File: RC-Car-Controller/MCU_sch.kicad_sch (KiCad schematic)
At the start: 15 parts, among them SW1 SW_Push, U7 STM32H743VGTx, Y1 Crystal

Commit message: Fixed Controller PCB
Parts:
- added C21: 2.2uF/10V, Capacitor_SMD:C_0201_0603Metric, symbol Device:C
- C10, C11, C12, C34, C35, C36, C7, C8, C9: footprint (none) -> Capacitor_SMD:C_0201_0603Metric
- C40: value 22uF/10V -> 2.2uF/10V; footprint (none) -> Capacitor_SMD:C_0201_0603Metric
- R11, R12: footprint (none) -> Resistor_SMD:R_0201_0603Metric
- SW1: footprint (none) -> Button_Switch_THT:SW_SPST_Omron_B3F-40xx
- Y1: footprint (none) -> Crystal:Crystal_SMD_Abracon_ABM3-2Pin_5.0x3.2mm
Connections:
- net +3V3: now also U7.20 (VREF+)
- net GND_3V3: now also C21.2
- net LEFT_PWM1: now reaches U7.22 (PA0)
- net LEFT_EN1: now reaches U7.23 (PA1)
- net LEFT_PWM2: now reaches U7.24 (PA2)
- net LEFT_EN2: now reaches U7.25 (PA3)
- net at C40.1, U7.73 (VCAP): no longer U7.48 (VCAP)
- net RIGHT_PWM1: now reaches U7.59 (PD12)
- net RIGHT_EN1: now reaches U7.60 (PD13)
- net RIGHT_PWM2: now reaches U7.89 (PB3)
- net RIGHT_EN2: now reaches U7.90 (PB4)
- net RELAY_CTRL: now reaches U7.93 (PB7)
- new net: C21.1, U7.48 (VCAP)
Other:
- moved on the sheet: C10, C11, C12, C7, C8, C9

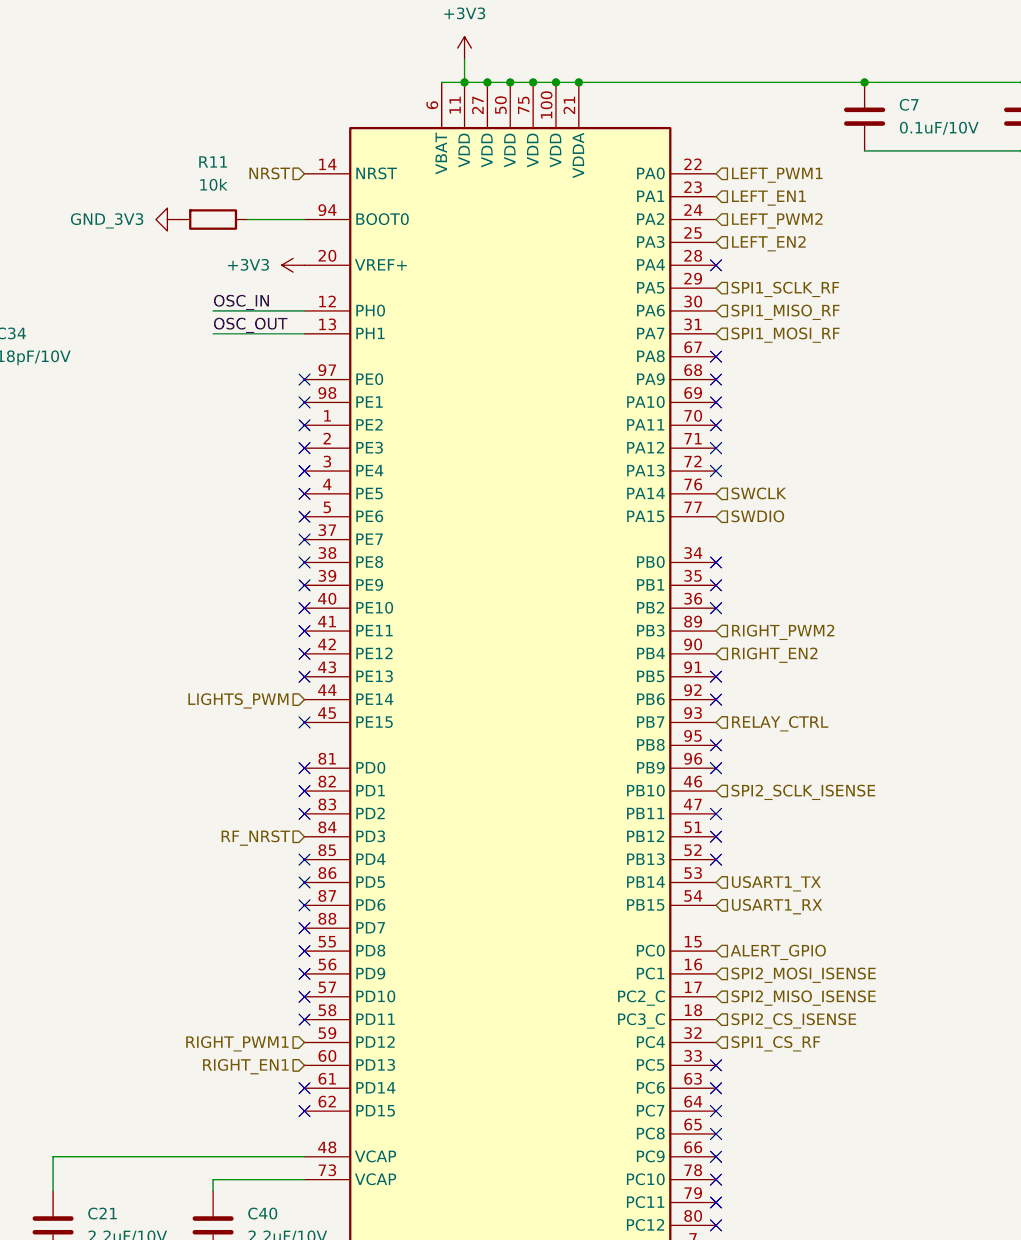
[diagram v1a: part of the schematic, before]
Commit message: Added IO to Controller
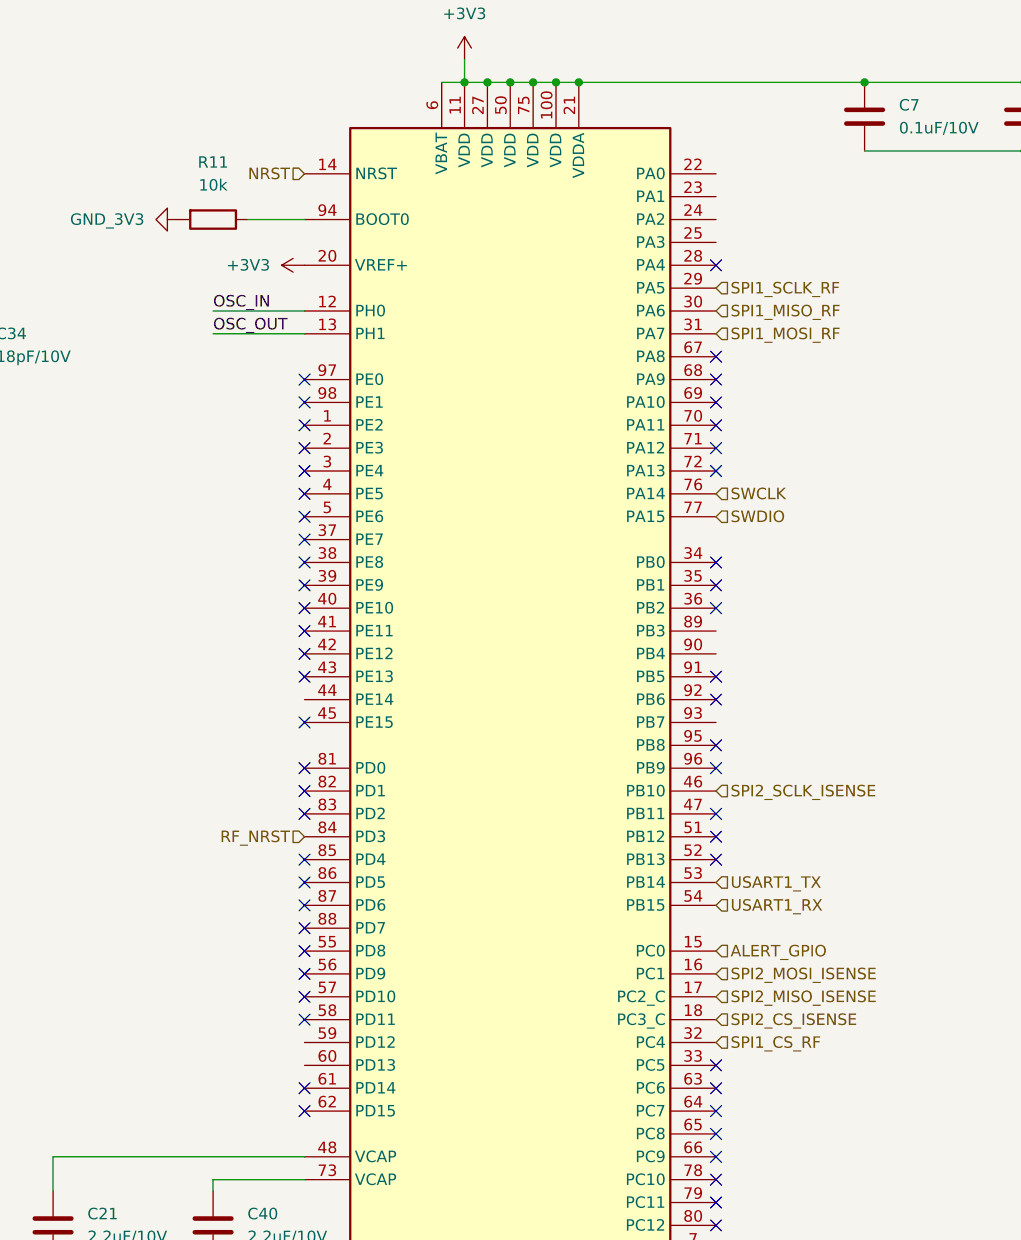
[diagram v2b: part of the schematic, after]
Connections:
- net LEFT_EN1: no longer names the net of U7.23 (PA1)
- net LEFT_EN2: no longer names the net of U7.25 (PA3)
- net LEFT_PWM1: no longer names the net of U7.22 (PA0)
- net LEFT_PWM2: no longer names the net of U7.24 (PA2)
- net LIGHTS_PWM: no longer names the net of U7.44 (PE14)
- net RELAY_CTRL: no longer names the net of U7.93 (PB7)
- net RIGHT_EN1: no longer names the net of U7.60 (PD13)
- net RIGHT_EN2: no longer names the net of U7.90 (PB4)
- net RIGHT_PWM1: no longer names the net of U7.59 (PD12)
- net RIGHT_PWM2: no longer names the net of U7.89 (PB3)
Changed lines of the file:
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@@
-		)
-	)
-	(hierarchical_label "RIGHT_PWM2"
-		(shape input)
-		(at 162.56 82.55 0)
-		(fields_autoplaced yes)
-		(effects
-			(font
-				(size 1.27 1.27)
-			)
-			(justify left)
 		)
 	)
@@
 		)
 	)
-	(hierarchical_label "RIGHT_EN2"
-		(shape input)
-		(at 162.56 85.09 0)
-		(fields_autoplaced yes)
-		(effects
-			(font
-				(size 1.27 1.27)
-			)
-			(justify left)
-		)
-	)
 	(hierarchical_label "SPI2_SCLK_ISENSE"
 		(shape input)
 		(at 162.56 100.33 0)
-		(fields_autoplaced yes)
-		(effects
-			(font
-				(size 1.27 1.27)
-			)
-			(justify left)
-		)
-	)
-	(hierarchical_label "LEFT_PWM2"
-		(shape input)
-		(at 162.56 36.83 0)
-		(fields_autoplaced yes)
-		(effects
-			(font
-				(size 1.27 1.27)
-			)
-			(justify left)
-		)
-	)
-	(hierarchical_label "LEFT_EN2"
-		(shape input)
-		(at 162.56 39.37 0)
 		(fields_autoplaced yes)
 		(effects
@@
 		)
 	)
-	(hierarchical_label "LEFT_PWM1"
-		(shape input)
-		(at 162.56 31.75 0)
-		(fields_autoplaced yes)
-		(effects
-			(font
-				(size 1.27 1.27)
-			)
-			(justify left)
-		)
-	)
-	(hierarchical_label "RIGHT_PWM1"
-		(shape input)
-		(at 116.84 128.27 180)
-		(fields_autoplaced yes)
-		(effects
-			(font
-				(size 1.27 1.27)
-			)
-			(justify right)
-		)
-	)
-	(hierarchical_label "LIGHTS_PWM"
-		(shape input)
-		(at 116.84 90.17 180)
-		(fields_autoplaced yes)
-		(effects
-			(font
-				(size 1.27 1.27)
-			)
-			(justify right)
-		)
-	)
-	(hierarchical_label "LEFT_EN1"
-		(shape input)
-		(at 162.56 34.29 0)
-		(fields_autoplaced yes)
-		(effects
-			(font
-				(size 1.27 1.27)
-			)
-			(justify left)
-		)
-	)
-	(hierarchical_label "RELAY_CTRL"
-		(shape input)
-		(at 162.56 92.71 0)
-		(fields_autoplaced yes)
-		(effects
-			(font
-				(size 1.27 1.27)
-			)
-			(justify left)
-		)
-	)
-	(hierarchical_label "RIGHT_EN1"
-		(shape input)
-		(at 116.84 130.81 180)
-		(fields_autoplaced yes)
-		(effects
-			(font
-				(size 1.27 1.27)
-			)
-			(justify right)
-		)
-	)

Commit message: Finished prelim. Controller
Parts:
- removed C34, C35, C36: 18pF/10V, Capacitor_SMD:C_0201_0603Metric, symbol Device:C
- removed C40: 2.2uF/10V, Capacitor_SMD:C_0201_0603Metric, symbol Device:C
- removed U7: STM32H743VGTx, Package_QFP:LQFP-100_14x14mm_P0.5mm, symbol MCU_ST_STM32H7:STM32H743VGTx
- added C13: 0.1uF/10V, Capacitor_SMD:C_0201_0603Metric, symbol Device:C
- added C4, C5, C6: 18pF/10V, Capacitor_SMD:C_0201_0603Metric, symbol Device:C
- added U4: STM32H743VGTx, Package_QFP:LQFP-100_14x14mm_P0.5mm, symbol MCU_ST_STM32H7:STM32H743VGTx
- C21: value 2.2uF/10V -> 0.1uF/10V
- C7, C8: value 0.1uF/10V -> 2.2uF/10V
- R11: value 10k -> 10kohm
- R12: value 10kohm -> 10k
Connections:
- net +3V3: now also C21.1, R11.1, C13.1, U4.100 (VDD), U4.11 (VDD), U4.20 (VREF+), U4.21 (VDDA), U4.27 (VDD), U4.50 (VDD), U4.6 (VBAT), U4.75 (VDD); no longer C7.1, C8.1, R12.1
- net ALERT_GPIO: now also U4.15 (PC0)
- net GND_3V3: now also R12.2, C13.2, C4.2, C5.2, C6.2, U4.10 (VSS), U4.19 (VSSA), U4.26 (VSS), U4.49 (VSS), U4.74 (VSS), U4.99 (VSS); no longer R11.2
- net NRST: now also R11.2, C5.1, U4.14 (NRST); no longer R12.2
- net OSC_IN: now also C4.1, U4.12 (PH0)
- net OSC_OUT: now also C6.1, U4.13 (PH1)
- net RF_NRST: now also U4.40 (PE10)
- net SWCLK: now also U4.76 (PA14)
- net SWDIO: now also U4.77 (PA15)
- net USART1_RX: now also U4.54 (PB15)
- net USART1_TX: now also U4.53 (PB14)
- new net: R12.1, U4.94 (BOOT0)
- new net: C7.1, U4.48 (VCAP)
- new net: C8.1, U4.73 (VCAP)
- new net BTN_L: U4.81 (PD0)
- new net BTN_R: U4.82 (PD1)
- new net I2C1_SCL: U4.92 (PB6)
- new net I2C1_SDA: U4.96 (PB9)
- new net I2C2_SCL: U4.46 (PB10)
- new net I2C2_SDA: U4.47 (PB11)
- new net SPI2_CS_LCD: U4.18 (PC3_C)
- new net SPI2_MISO: U4.17 (PC2_C)
- new net SPI2_MOSI: U4.16 (PC1)
- new net SPI2_SCLK: U4.52 (PB13)
- new net SPI3_CS_ADC: U4.80 (PC12)
- new net SPI3_MISO: U4.79 (PC11)
- new net SPI3_MOSI: U4.36 (PB2)
- new net SPI3_SCLK: U4.78 (PC10)
- new net SPI4_CS_RF: U4.41 (PE11)
- new net SPI4_MISO_RF: U4.43 (PE13)
- new net SPI4_MOSI_RF: U4.5 (PE6)
- new net SPI4_SCLK_RF: U4.42 (PE12)
- new net WIPE_L: U4.31 (PA7)
- new net WIPE_R: U4.34 (PB0)
- no-connect marks 56 -> 54

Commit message: Did some stuff on the Controller
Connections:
- net at R12.1: no longer U4.94 (BOOT0)
- net MCU_USB_D-: now reaches U4.70 (PA11)
- net MCU_USB_D+: now reaches U4.71 (PA12)
- no-connect marks 54 -> 52
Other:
- note added: "Turn this into a DIP Switch. Want to be able to prog with USB"
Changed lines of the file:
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@@
-	)
-	(no_connect
-		(at 143.51 71.12)
 	)
 	(no_connect
@@
 	)
 	(no_connect
-		(at 143.51 73.66)
-	)
-	(no_connect
 		(at 97.79 139.7)
 	)
@@
 	(wire
 		(pts
-			(xy 91.44 48.26) (xy 97.79 48.26)
-		)
-		(stroke
-			(width 0)
-			(type default)
-		)
-	)
-	(wire
-		(pts
 			(xy 40.64 58.42) (xy 46.99 58.42)
 		)
@@
 			(width 0)
 			(type default)
+		)
+	)
+	(text "Turn this into a DIP Switch.\nWant to be able to prog with USB"
+		(exclude_from_sim no)
+		(at 67.31 44.45 0)
+		(effects
+			(font
+				(size 1.27 1.27)
+			)
 		)
 	)
@@
 		)
 	)
+	(hierarchical_label "MCU_USB_D+"
+		(shape input)
+		(at 143.51 73.66 0)
+		(fields_autoplaced yes)
+		(effects
+			(font
+				(size 1.27 1.27)
+			)
+			(justify left)
+		)
+	)
 	(hierarchical_label "NRST"
 		(shape input)
@@
 		(fields_autoplaced yes)
 		(effects
+			(font
+				(size 1.27 1.27)
+			)
+			(justify left)
+		)
+	)
+	(hierarchical_label "MCU_USB_D-"
+		(shape input)
+		(at 143.51 71.12 0)
+		(fields_autoplaced yes)
+		(effects

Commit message: Did power schtuff
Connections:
- net WIPE_L: no longer U4.31 (PA7)
- net WIPE_R: no longer U4.34 (PB0)
- net SPI4_SCLK: now reaches U4.1 (PE2)
- net SPI1_SCLK: now reaches U4.29 (PA5)
- net SPI1_MISO: now reaches U4.30 (PA6)
- net SPI1_CS: now reaches U4.32 (PC4)
- net SPI1_DC: now reaches U4.33 (PC5)
- net SPI4_MISO: now reaches U4.4 (PE5)
- net I2C3_SDA: now reaches U4.66 (PC9)
- net I2C3_SCL: now reaches U4.67 (PA8)
- net RF_NRST: no longer names the net of U4.40 (PE10)
- net SPI2_CS_LCD: no longer names the net of U4.18 (PC3_C)
- net SPI2_MISO: no longer names the net of U4.17 (PC2_C)
- net SPI2_MOSI: no longer names the net of U4.16 (PC1)
- net SPI2_SCLK: no longer names the net of U4.52 (PB13)
- net SPI3_CS_ADC: no longer names the net of U4.80 (PC12)
- net SPI3_MISO: no longer names the net of U4.79 (PC11)
- net SPI3_MOSI: no longer names the net of U4.36 (PB2)
- net SPI3_SCLK: no longer names the net of U4.78 (PC10)
- net SPI4_CS_RF: no longer names the net of U4.41 (PE11)
- net SPI4_MISO_RF: no longer names the net of U4.43 (PE13)
- net SPI4_MOSI_RF renamed SPI4_MOSI
- net SPI4_SCLK_RF: no longer names the net of U4.42 (PE12)
- new net SPI1_MOSI: U4.31 (PA7)
- no-connect marks 52 -> 57

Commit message: Did a bunch of stuff on the controller
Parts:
- added R19, R20, R5, R6: 4.7kohm, Resistor_SMD:R_0603_1608Metric, symbol Device:R
- C10, C11, C12, C13, C21, C4, C5, C6, C7, C8, C9: footprint Capacitor_SMD:C_0201_0603Metric -> Capacitor_SMD:C_0603_1608Metric
- R11, R12: footprint Resistor_SMD:R_0201_0603Metric -> Capacitor_SMD:C_0603_1608Metric
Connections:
- net +3V3: now also R19.2, R20.2, R5.2, R6.2
- net BTN_L: no longer U4.81 (PD0)
- net BTN_R: no longer U4.82 (PD1)
- net I2C1_SCL: now also R5.1
- net I2C1_SDA: now also R6.1
- net I2C2_SCL: now also R19.1
- net I2C2_SDA: now also R20.1
- net SWCLK: no longer U4.76 (PA14)
- net SWDIO: no longer U4.77 (PA15)
- net SPI4_CS: now reaches U4.3 (PE4)
- net SDMMC1_D0: now reaches U4.65 (PC8)
- net SDMMC1_D2: now reaches U4.78 (PC10)
- net SDMMC1_D3: now reaches U4.79 (PC11)
- net SDMMC1_CK: now reaches U4.80 (PC12)
- net SDMMC1_CMD: now reaches U4.83 (PD2)
- net I2C3_SCL: no longer names the net of U4.67 (PA8)
- net I2C3_SDA renamed SDMMC1_D1
- net SPI1_CS: no longer names the net of U4.32 (PC4)
- net SPI1_DC: no longer names the net of U4.33 (PC5)
- net SPI1_MISO: no longer names the net of U4.30 (PA6)
- net SPI1_MOSI: no longer names the net of U4.31 (PA7)
- net SPI1_SCLK: no longer names the net of U4.29 (PA5)
- net SPI4_MISO renamed SPI4_DC
- no-connect marks 57 -> 61

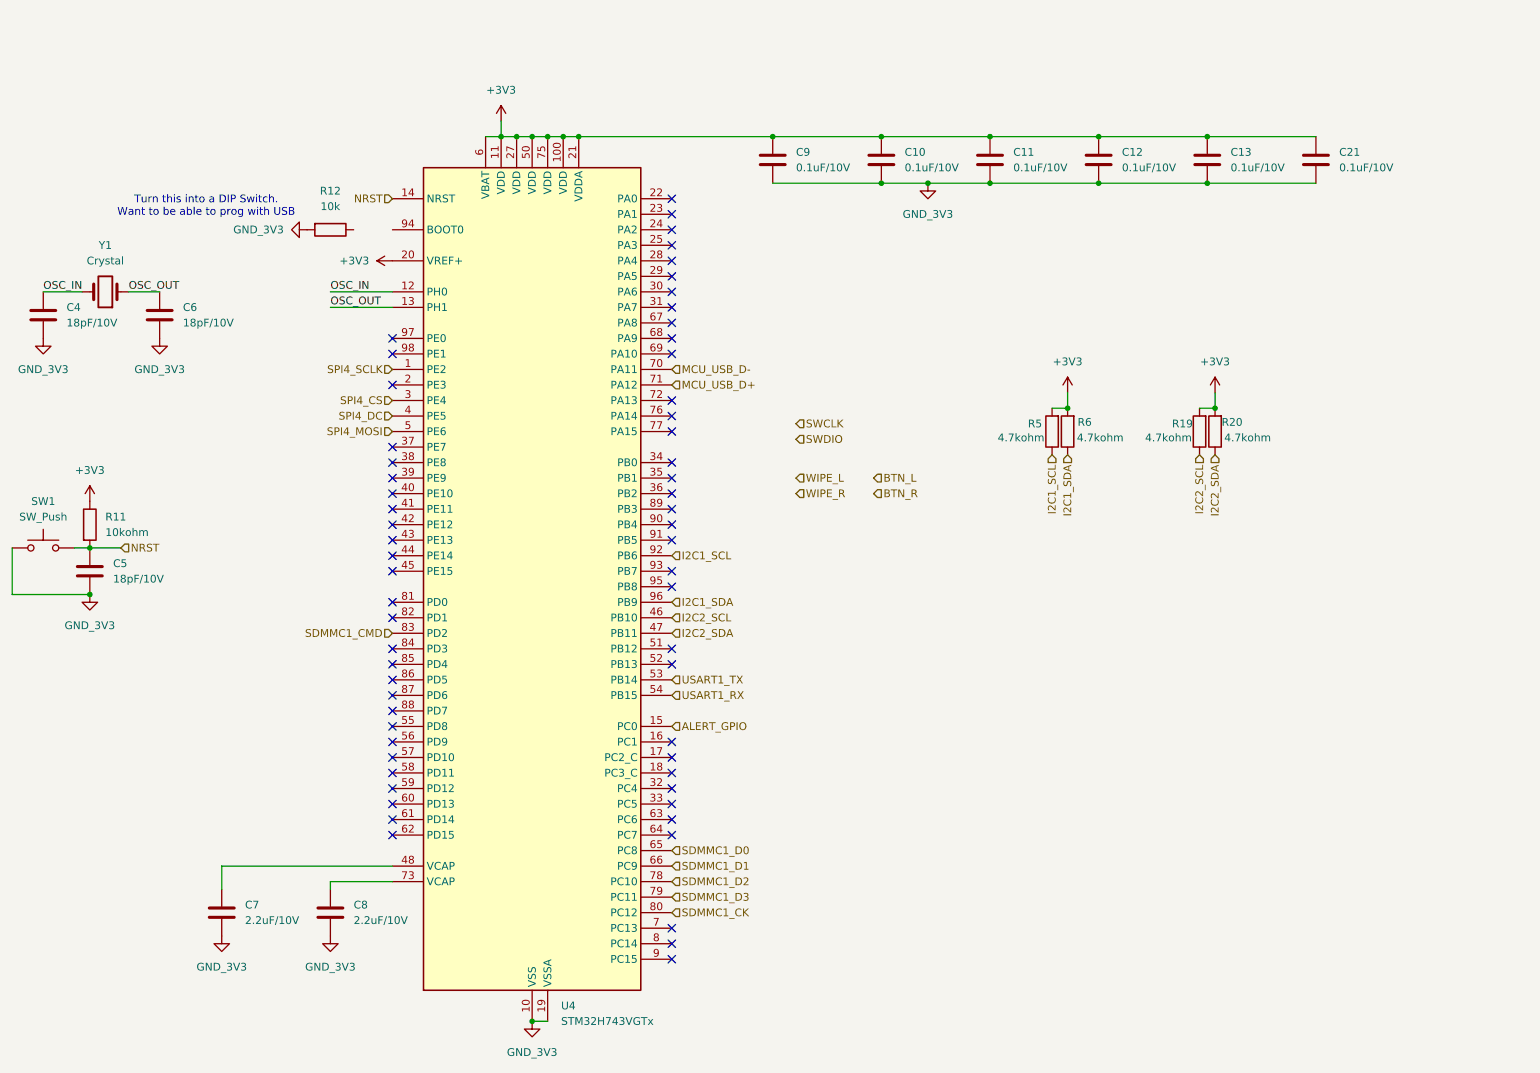
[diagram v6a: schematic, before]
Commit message: Finished non-RF Controller PCB
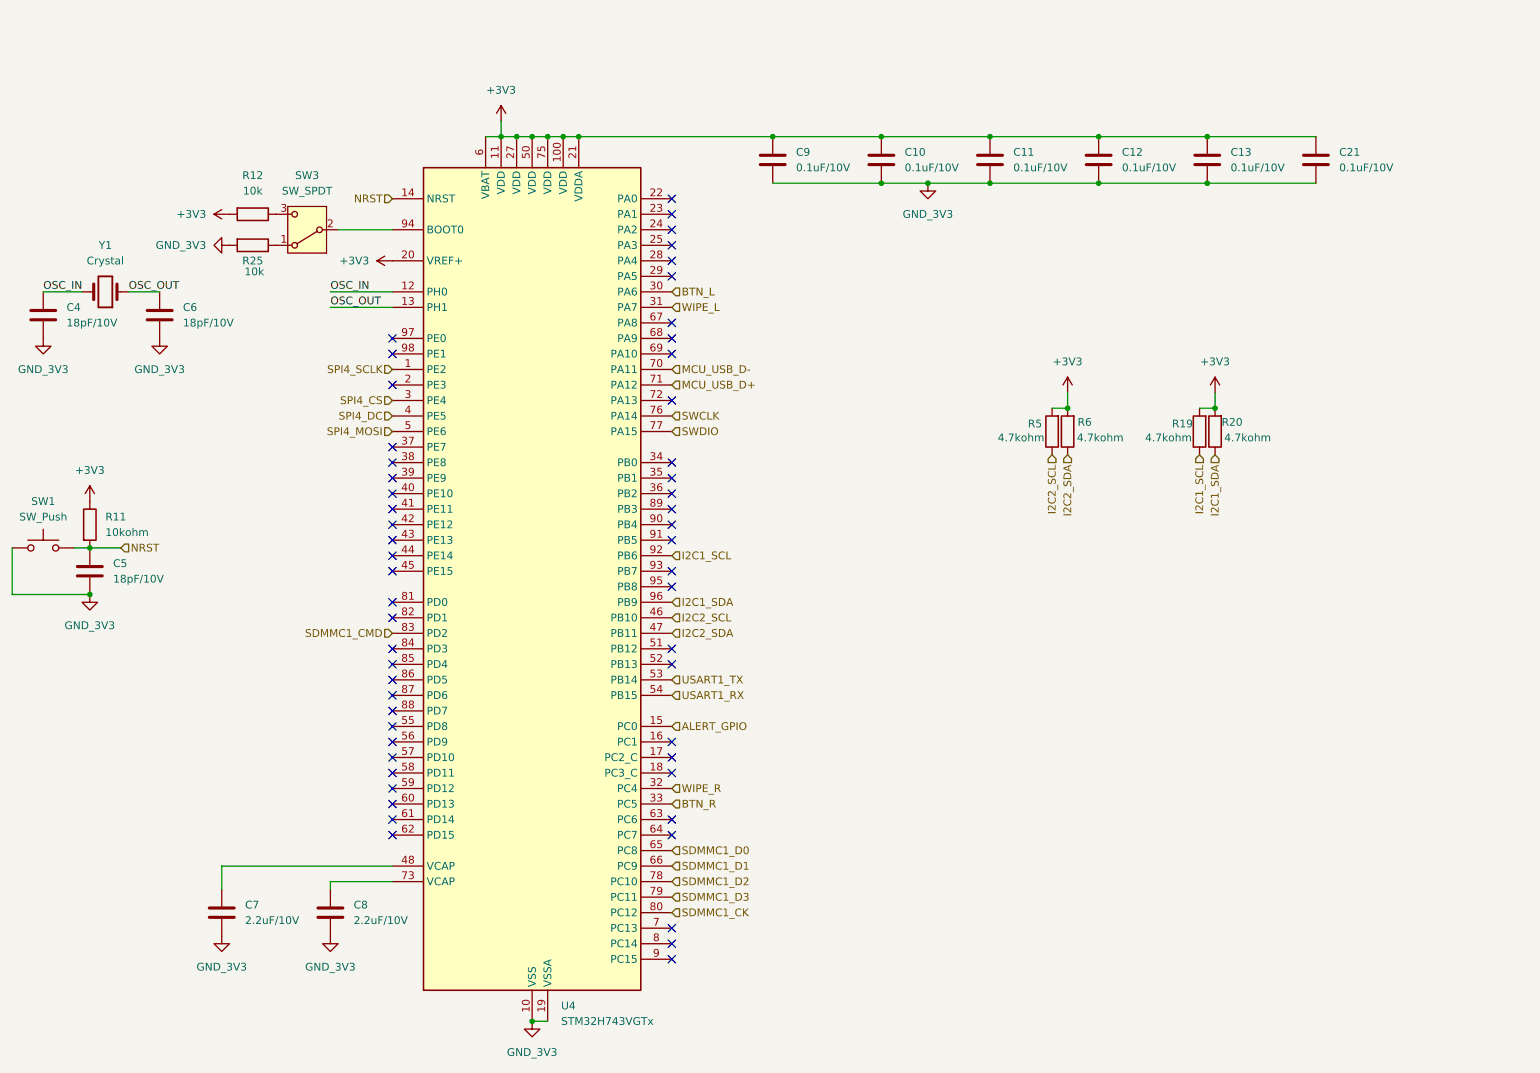
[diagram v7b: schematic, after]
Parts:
- added R25: 10k, Capacitor_SMD:C_0603_1608Metric, symbol Device:R
- added SW3: SW_SPDT, Connector_PinHeader_2.54mm:PinHeader_1x03_P2.54mm_Vertical, symbol Switch:SW_SPDT
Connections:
- net +3V3: now also R12.2
- net BTN_L: now also U4.30 (PA6)
- net BTN_R: now also U4.33 (PC5)
- net GND_3V3: now also R25.2; no longer R12.2
- net I2C1_SCL: now also R19.1; no longer R5.1
- net I2C1_SDA: now also R20.1; no longer R6.1
- net I2C2_SCL: now also R5.1; no longer R19.1
- net I2C2_SDA: now also R6.1; no longer R20.1
- net SWCLK: now also U4.76 (PA14)
- net SWDIO: now also U4.77 (PA15)
- net WIPE_L: now also U4.31 (PA7)
- net WIPE_R: now also U4.32 (PC4)
- net at R12.1: now also SW3.3 (C)
- net at U4.94 (BOOT0): now also SW3.2 (B)
- new net: R25.1, SW3.1 (A)
- no-connect marks 61 -> 55
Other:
- note removed: "Turn this into a DIP Switch. Want to be able to prog with USB"
- moved on the sheet: R12
